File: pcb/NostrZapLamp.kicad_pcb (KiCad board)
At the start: 2 copper layers, 41.9 x 52.3 mm, 5 parts, among them J1 LED, J2 Button, U1 ESP32_DevKit_V1_DOIT

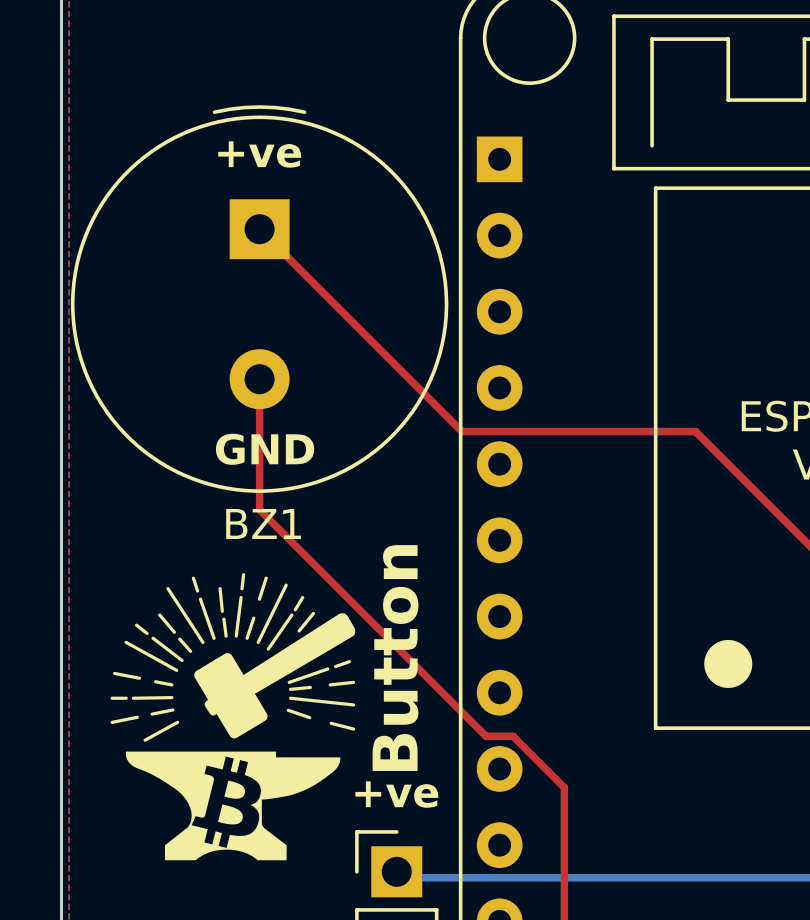
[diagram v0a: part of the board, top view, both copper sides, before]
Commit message: Change PCB holes to wider spacing for buzzer
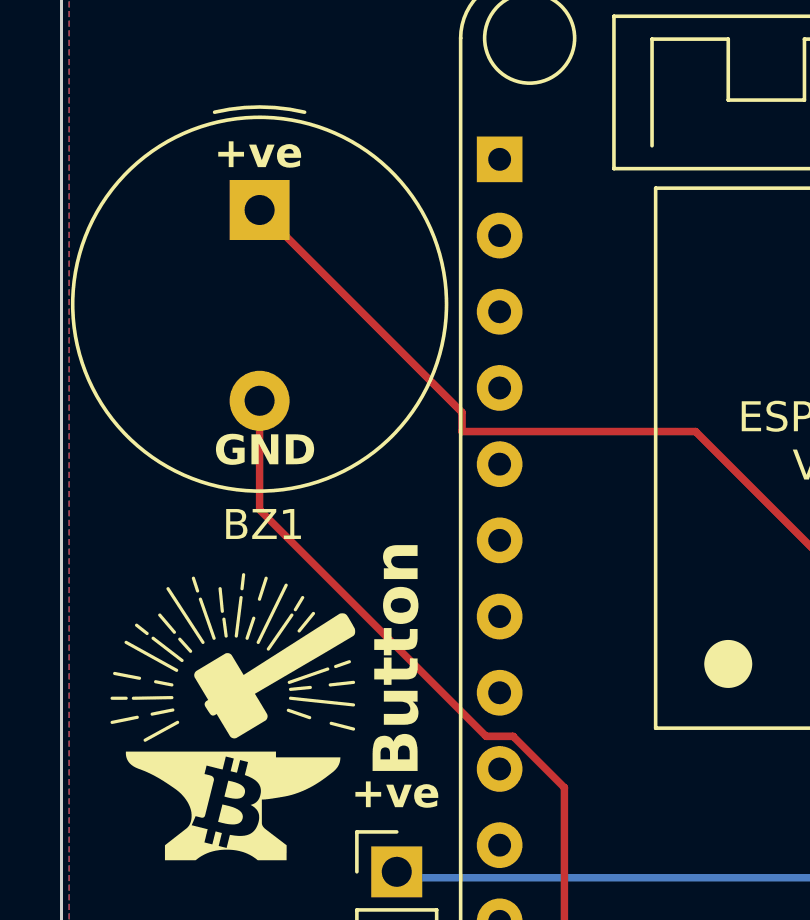
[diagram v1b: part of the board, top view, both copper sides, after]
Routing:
- net Net-(BZ1-+): track 40.5 -> 39.8 mm
- net Net-(BZ1--): track 44.0 -> 44.6 mm
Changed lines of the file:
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@@
     (fp_circle (center 2.5 0) (end 8.6 0)
       (stroke (width 0.1) (type solid)) (fill none) (layer "F.Fab"))
-    (pad "1" thru_hole rect (at 0 0 270) (size 2 2) (drill 1) (layers "*.Cu" "*.Mask")
+    (pad "1" thru_hole rect (at -0.64 0 270) (size 2 2) (drill 1) (layers "*.Cu" "*.Mask")
       (net 29 "Net-(BZ1--)") (pinfunction "-") (pintype "passive"))
-    (pad "2" thru_hole circle (at 5 0 270) (size 2 2) (drill 1) (layers "*.Cu" "*.Mask")
+    (pad "2" thru_hole circle (at 5.72 0 270) (size 2 2) (drill 1) (layers "*.Cu" "*.Mask")
       (net 30 "Net-(BZ1-+)") (pinfunction "+") (pintype "passive"))
     (model "${KICAD6_3DMODEL_DIR}/Buzzer_Beeper.3dshapes/Buzzer_TDK_PS1240P02BT_D12.2mm_H6.5mm.wrl"
@@
   (segment (start 122.682 104.902) (end 144.78 104.902) (width 0.25) (layer "B.Cu") (net 3))
   (segment (start 121.806784 84.638) (end 129.596 84.638) (width 0.25) (layer "F.Cu") (net 29))
-  (segment (start 115.062 77.893216) (end 121.806784 84.638) (width 0.25) (layer "F.Cu") (net 29))
+  (segment (start 121.806784 84.638) (end 121.806784 83.998) (width 0.25) (layer "F.Cu") (net 29))
+  (segment (start 121.806784 83.998) (end 115.062 77.253216) (width 0.25) (layer "F.Cu") (net 29))
   (segment (start 129.596 84.638) (end 148.463 103.505) (width 0.25) (layer "F.Cu") (net 29))
+  (segment (start 115.062 87.247251) (end 115.062 83.613216) (width 0.25) (layer "F.Cu") (net 30))
   (segment (start 125.222 106.426) (end 123.063 108.585) (width 0.25) (layer "F.Cu") (net 30))
-  (segment (start 115.062 82.893216) (end 115.062 87.247251) (width 0.25) (layer "F.Cu") (net 30))
   (segment (start 123.513251 94.798) (end 125.222 96.506749) (width 0.25) (layer "F.Cu") (net 30))
-  (segment (start 115.062 87.247251) (end 122.612749 94.798) (width 0.25) (layer "F.Cu") (net 30))
   (segment (start 125.222 96.506749) (end 125.222 106.426) (width 0.25) (layer "F.Cu") (net 30))
+  (segment (start 122.612749 94.798) (end 115.062 87.247251) (width 0.25) (layer "F.Cu") (net 30))
   (segment (start 122.612749 94.798) (end 123.513251 94.798) (width 0.25) (layer "F.Cu") (net 30))
   (segment (start 121.976 113.995) (end 121.976 109.672) (width 0.25) (layer "B.Cu") (net 30))
